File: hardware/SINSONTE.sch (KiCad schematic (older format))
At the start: 20 parts, among them J1 BAT, J2 CLOCK, J3 LIGHT_SENSOR, J4 Conn_01x17_Male, Q1 2N7000, Q2 PN2222A, SW1 SW_Push, U1 Pico

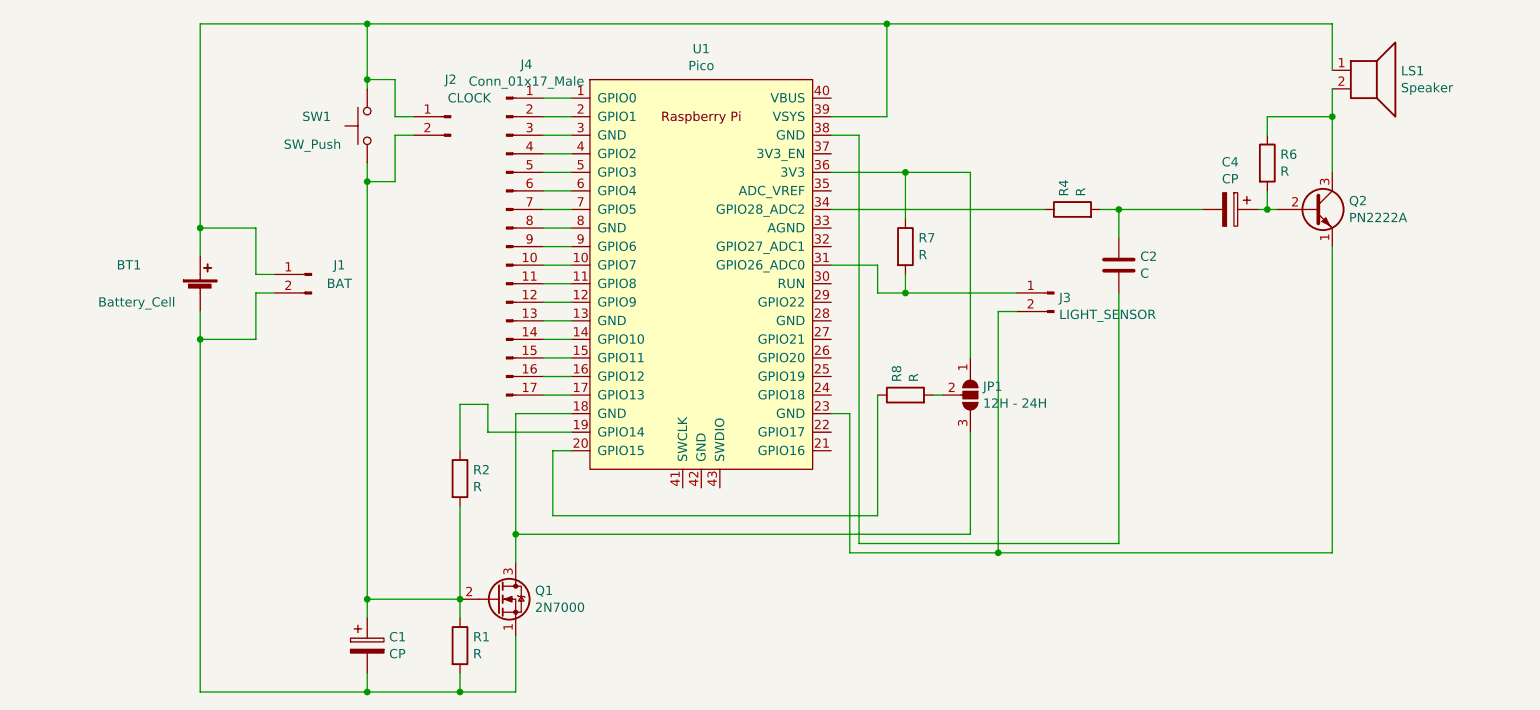
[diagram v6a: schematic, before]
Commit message: changed autopower off strategy
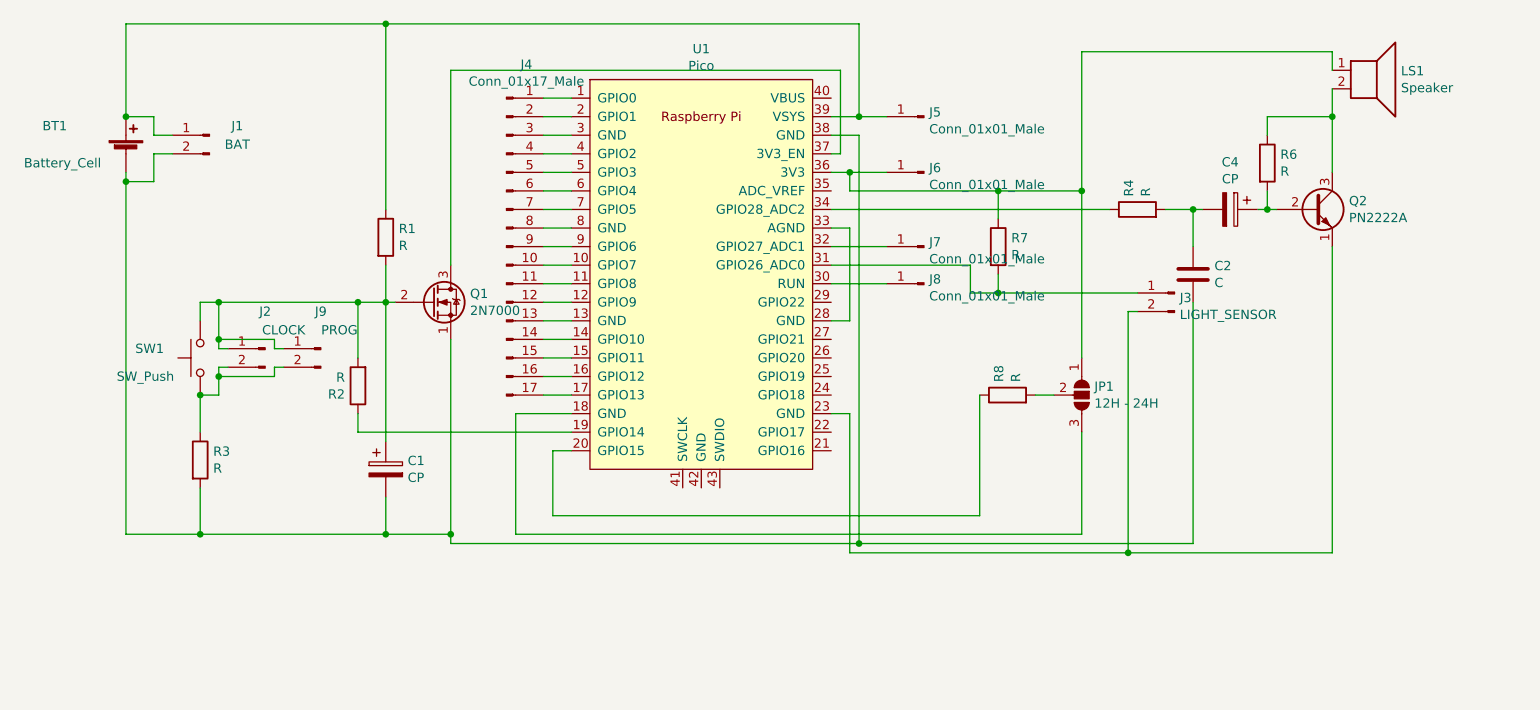
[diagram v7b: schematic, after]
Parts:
- added J5, J6, J7, J8: Conn_01x01_Male, Connector_PinHeader_2.54mm:PinHeader_1x01_P2.54mm_Vertical, symbol Connector:Conn_01x01_Male
- added J9: PROG, Connector_PinHeader_2.54mm:PinHeader_1x02_P2.54mm_Vertical, symbol Connector:Conn_01x02_Male
- added R3: R, Resistor_THT:R_Axial_DIN0204_L3.6mm_D1.6mm_P2.54mm_Vertical, symbol Device:R
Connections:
- net at JP1.3 (B), U1.18 (GND): no longer Q1.3 (D)
- net at U1.28 (GND): now also U1.33 (AGND)
- net at U1.30 (RUN): now also J8.1 (Pin_1)
- net at U1.32 (GPIO27_ADC1): now also J7.1 (Pin_1)
- net at JP1.1 (A), R7.1, U1.36 (3V3): now also LS1.1, J6.1 (Pin_1)
- net at U1.37 (3V3_EN): now also Q1.3 (D)
- net at C2.2, U1.38 (GND): now also BT1.2 (-), C1.2, J1.2 (Pin_2), Q1.1 (S), R3.2
- net at BT1.1 (+), J1.1 (Pin_1), U1.39 (VSYS): now also R1.1, J5.1 (Pin_1); no longer J2.1 (Pin_1), LS1.1, SW1.1
- net at C1.1, Q1.2 (G), R2.2: now also J2.1 (Pin_1), R1.2, SW1.1, J9.1 (Pin_1); no longer J2.2 (Pin_2), R1.1, SW1.2
- new net: J2.2 (Pin_2), J9.2 (Pin_2), R3.1, SW1.2
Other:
- moved on the sheet: BT1, C1, C2, J1, J2, J3, JP1, Q1, R1, R2, R4, R7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

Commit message: all expansion headers placed
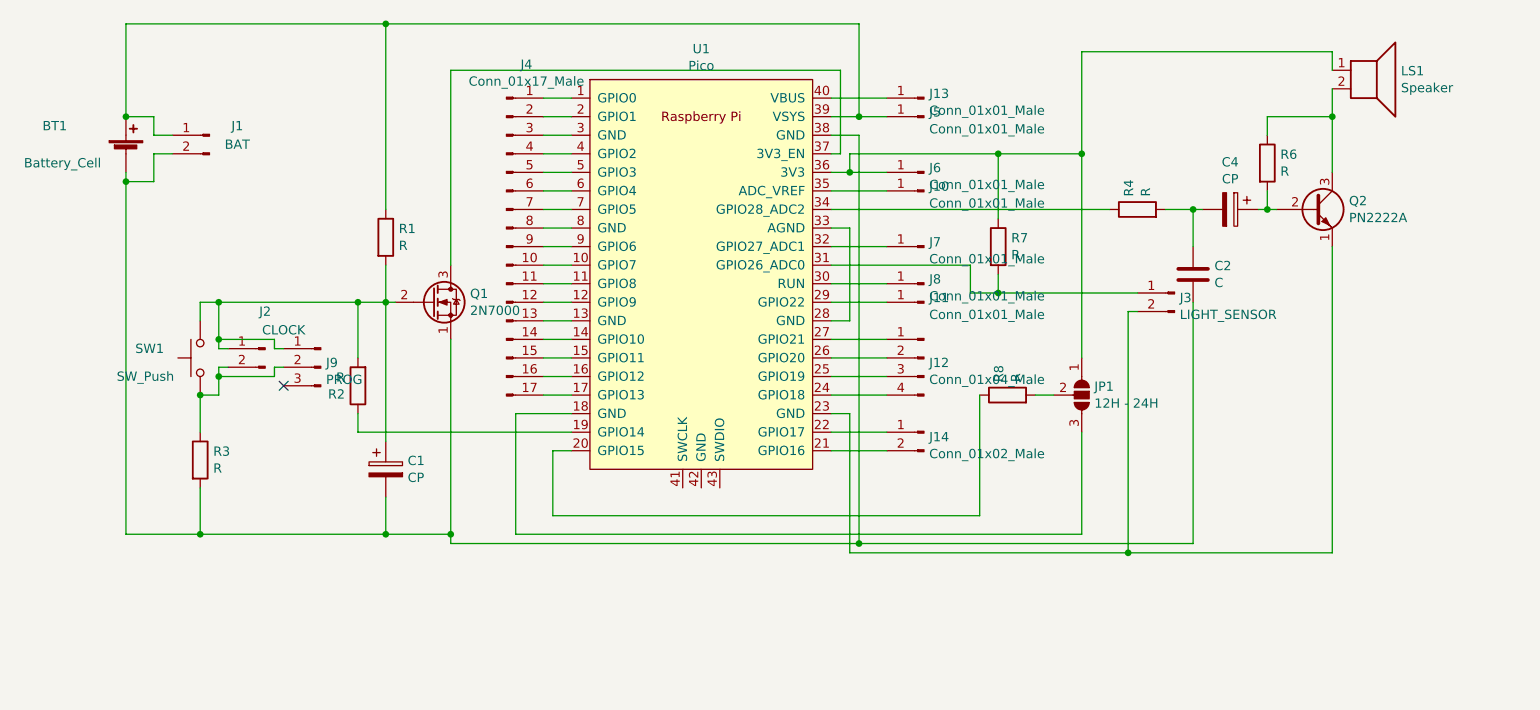
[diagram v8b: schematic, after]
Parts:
- removed J9: PROG, Connector_PinHeader_2.54mm:PinHeader_1x02_P2.54mm_Vertical, symbol Connector:Conn_01x02_Male
- added J10, J11, J13: Conn_01x01_Male, Connector_PinHeader_2.54mm:PinHeader_1x01_P2.54mm_Vertical, symbol Connector:Conn_01x01_Male
- added J12: Conn_01x04_Male, Connector_PinHeader_2.54mm:PinHeader_1x04_P2.54mm_Vertical, symbol Connector:Conn_01x04_Male
- added J14: Conn_01x02_Male, Connector_PinHeader_2.54mm:PinHeader_1x02_P2.54mm_Vertical, symbol Connector:Conn_01x02_Male
- added J9: PROG, Connector_PinHeader_2.54mm:PinHeader_1x03_P2.54mm_Vertical, symbol Connector:Conn_01x03_Male
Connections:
- net at U1.21 (GPIO16): now also J14.2 (Pin_2)
- net at U1.22 (GPIO17): now also J14.1 (Pin_1)
- net at U1.24 (GPIO18): now also J12.4 (Pin_4)
- net at U1.25 (GPIO19): now also J12.3 (Pin_3)
- net at U1.26 (GPIO20): now also J12.2 (Pin_2)
- net at U1.27 (GPIO21): now also J12.1 (Pin_1)
- net at U1.29 (GPIO22): now also J11.1 (Pin_1)
- net at U1.35 (ADC_VREF): now also J10.1 (Pin_1)
- net at U1.40 (VBUS): now also J13.1 (Pin_1)
- net at C1.1, J2.1 (Pin_1), Q1.2 (G)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: now also J9.1 (Pin_1)
- net at J2.2 (Pin_2), R3.1, SW1.2: now also J9.2 (Pin_2)
- no-connect marks 0 -> 1
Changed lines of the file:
@@
 $EndComp
 Wire Wire Line
-	7200 3050 7200 3200
+	7200 2850 7200 3200
 Wire Wire Line
 	6300 3450 7050 3450
@@
 	6300 2750 6450 2750
 Wire Wire Line
-	6450 2750 6450 4950
-Wire Wire Line
 	8650 2750 8650 2650
 Wire Wire Line
@@
 	4600 4900 7650 4900
 Wire Wire Line
-	7200 3050 7650 3050
+	7200 2850 7650 2850
 Wire Wire Line
 	4800 4800 7100 4800
@@
 Connection ~ 6450 2650
 Wire Wire Line
-	7650 3050 7650 3950
-Wire Wire Line
-	7200 3050 6400 3050
-Wire Wire Line
-	6400 3050 6400 2950
+	7650 2850 7650 3950
+Wire Wire Line
+	7200 2850 6400 2850
 Wire Wire Line
 	6400 2950 6300 2950
-Connection ~ 7200 3050
+Connection ~ 7200 2850
 $Comp
 L Connector:Conn_01x01_Male J6
@@
 	9000 2300 7650 2300
 Wire Wire Line
-	7650 2300 7650 3050
-Connection ~ 7650 3050
+	7650 2300 7650 2850
+Connection ~ 7650 2850
 Wire Wire Line
 	4600 4250 4600 4900
@@
 Wire Wire Line
 	4250 2400 4250 3450
-$Comp
-L Connector:Conn_01x02_Male J9
-U 1 1 607093E7
-P 3550 3900
-F 0 "J9" H 3550 4100 50  0000 C CNN
-F 1 "PROG" H 3450 4000 50  0000 C CNN
-F 2 "Connector_PinHeader_2.54mm:PinHeader_1x02_P2.54mm_Vertical" H 3550 3900 50  0001 C CNN
-F 3 "~" H 3550 3900 50  0001 C CNN
-	1    3550 3900
-	-1   0    0    -1
-$EndComp
 Connection ~ 3900 2150
 Wire Wire Line
@@
 	2500 3000 2500 4900
 Wire Wire Line
-	3000 3900 3000 3850
-Wire Wire Line
 	3050 4000 3000 4000
-Wire Wire Line
-	3000 4000 3000 4050
 Wire Wire Line
 	3000 4150 2900 4150
@@
 	3750 3650 3900 3650
 Wire Wire Line
-	3350 4000 3300 4000
-Wire Wire Line
-	3300 4000 3300 4050
-Wire Wire Line
-	3300 4050 3000 4050
-Connection ~ 3000 4050
-Wire Wire Line
-	3000 4050 3000 4150
-Wire Wire Line
-	3350 3900 3300 3900
-Wire Wire Line
-	3300 3900 3300 3850
-Wire Wire Line
-	3300 3850 3000 3850
-Connection ~ 3000 3850
-Wire Wire Line
-	3000 3850 3000 3650
-Wire Wire Line
 	6450 4950 4250 4950
 Wire Wire Line
@@
 Connection ~ 6450 4950
 Connection ~ 4250 4900
+Wire Wire Line
+	6400 2850 6400 2950
+$Comp
+L Connector:Conn_01x01_Male J10
+U 1 1 6082CC33
+P 6800 3050
+F 0 "J10" H 6772 3074 50  0000 R CNN
+F 1 "Conn_01x01_Male" H 6772 2983 50  0000 R CNN
+F 2 "Connector_PinHeader_2.54mm:PinHeader_1x01_P2.54mm_Vertical" H 6800 3050 50  0001 C CNN
+F 3 "~" H 6800 3050 50  0001 C CNN
+	1    6800 3050
+	-1   0    0    -1
+$EndComp
+Wire Wire Line
+	6300 3050 6600 3050
+$Comp
+L Connector:Conn_01x01_Male J11
+U 1 1 60836840
+P 6800 3650
+F 0 "J11" H 6772 3674 50  0000 R CNN
+F 1 "Conn_01x01_Male" H 6772 3583 50  0000 R CNN
+F 2 "Connector_PinHeader_2.54mm:PinHeader_1x01_P2.54mm_Vertical" H 6800 3650 50  0001 C CNN
+F 3 "~" H 6800 3650 50  0001 C CNN
+	1    6800 3650
+	-1   0    0    -1
+$EndComp
+Wire Wire Line
+	6300 3650 6600 3650
+Wire Wire Line
+	6450 2750 6450 4950
+$Comp
+L Connector:Conn_01x04_Male J12
+U 1 1 6084391D
+P 6800 3950
+F 0 "J12" H 6772 3924 50  0000 R CNN
+F 1 "Conn_01x04_Male" H 6772 3833 50  0000 R CNN
+F 2 "Connector_PinHeader_2.54mm:PinHeader_1x04_P2.54mm_Vertical" H 6800 3950 50  0001 C CNN
+F 3 "~" H 6800 3950 50  0001 C CNN
+	1    6800 3950
+	-1   0    0    -1
+$EndComp
+Wire Wire Line
+	6300 3850 6600 3850
+Wire Wire Line
+	6300 3950 6600 3950
+Wire Wire Line
+	6300 4050 6600 4050
+Wire Wire Line
+	6300 4150 6600 4150
+$Comp
+L Connector:Conn_01x01_Male J13
+U 1 1 60872957
+P 6800 2550
+F 0 "J13" H 6772 2574 50  0000 R CNN
+F 1 "Conn_01x01_Male" H 6772 2483 50  0000 R CNN
+F 2 "Connector_PinHeader_2.54mm:PinHeader_1x01_P2.54mm_Vertical" H 6800 2550 50  0001 C CNN
+F 3 "~" H 6800 2550 50  0001 C CNN
+	1    6800 2550
+	-1   0    0    -1
+$EndComp
+Wire Wire Line
+	6300 2550 6600 2550
+$Comp
+L Connector:Conn_01x03_Male J9
+U 1 1 60882A91
+P 3550 4000
+F 0 "J9" H 3522 4024 50  0000 R CNN
+F 1 "PROG" H 3522 3933 50  0000 R CNN
+F 2 "Connector_PinHeader_2.54mm:PinHeader_1x03_P2.54mm_Vertical" H 3550 4000 50  0001 C CNN
+F 3 "~" H 3550 4000 50  0001 C CNN
+	1    3550 4000
+	-1   0    0    -1
+$EndComp
+Wire Wire Line
+	3000 3650 3000 3850
+Wire Wire Line
+	3350 3900 3300 3900
+Wire Wire Line
+	3300 3900 3300 3850
+Wire Wire Line
+	3300 3850 3000 3850
+Connection ~ 3000 3850
+Wire Wire Line
+	3000 3850 3000 3900
+Wire Wire Line
+	3000 4000 3000 4050
+Wire Wire Line
+	3350 4000 3300 4000
+Wire Wire Line
+	3300 4000 3300 4050
+Wire Wire Line
+	3300 4050 3000 4050
+Connection ~ 3000 4050
+Wire Wire Line
+	3000 4050 3000 4150
+NoConn ~ 3350 4100
+$Comp
+L Connector:Conn_01x02_Male J14
+U 1 1 608B2996
+P 6800 4350
+F 0 "J14" H 6772 4324 50  0000 R CNN
+F 1 "Conn_01x02_Male" H 6772 4233 50  0000 R CNN
+F 2 "Connector_PinHeader_2.54mm:PinHeader_1x02_P2.54mm_Vertical" H 6800 4350 50  0001 C CNN
+F 3 "~" H 6800 4350 50  0001 C CNN
+	1    6800 4350
+	-1   0    0    -1
+$EndComp
+Wire Wire Line
+	6300 4350 6600 4350
+Wire Wire Line
+	6300 4450 6600 4450
 $EndSCHEMATC
